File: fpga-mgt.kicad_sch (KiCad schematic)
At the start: 35 parts, among them U34 XCAU25P-2FFVB676I, U39 SI5319C-C-GM-ND, Y4 Resonator_114.285MHZ_ABM8

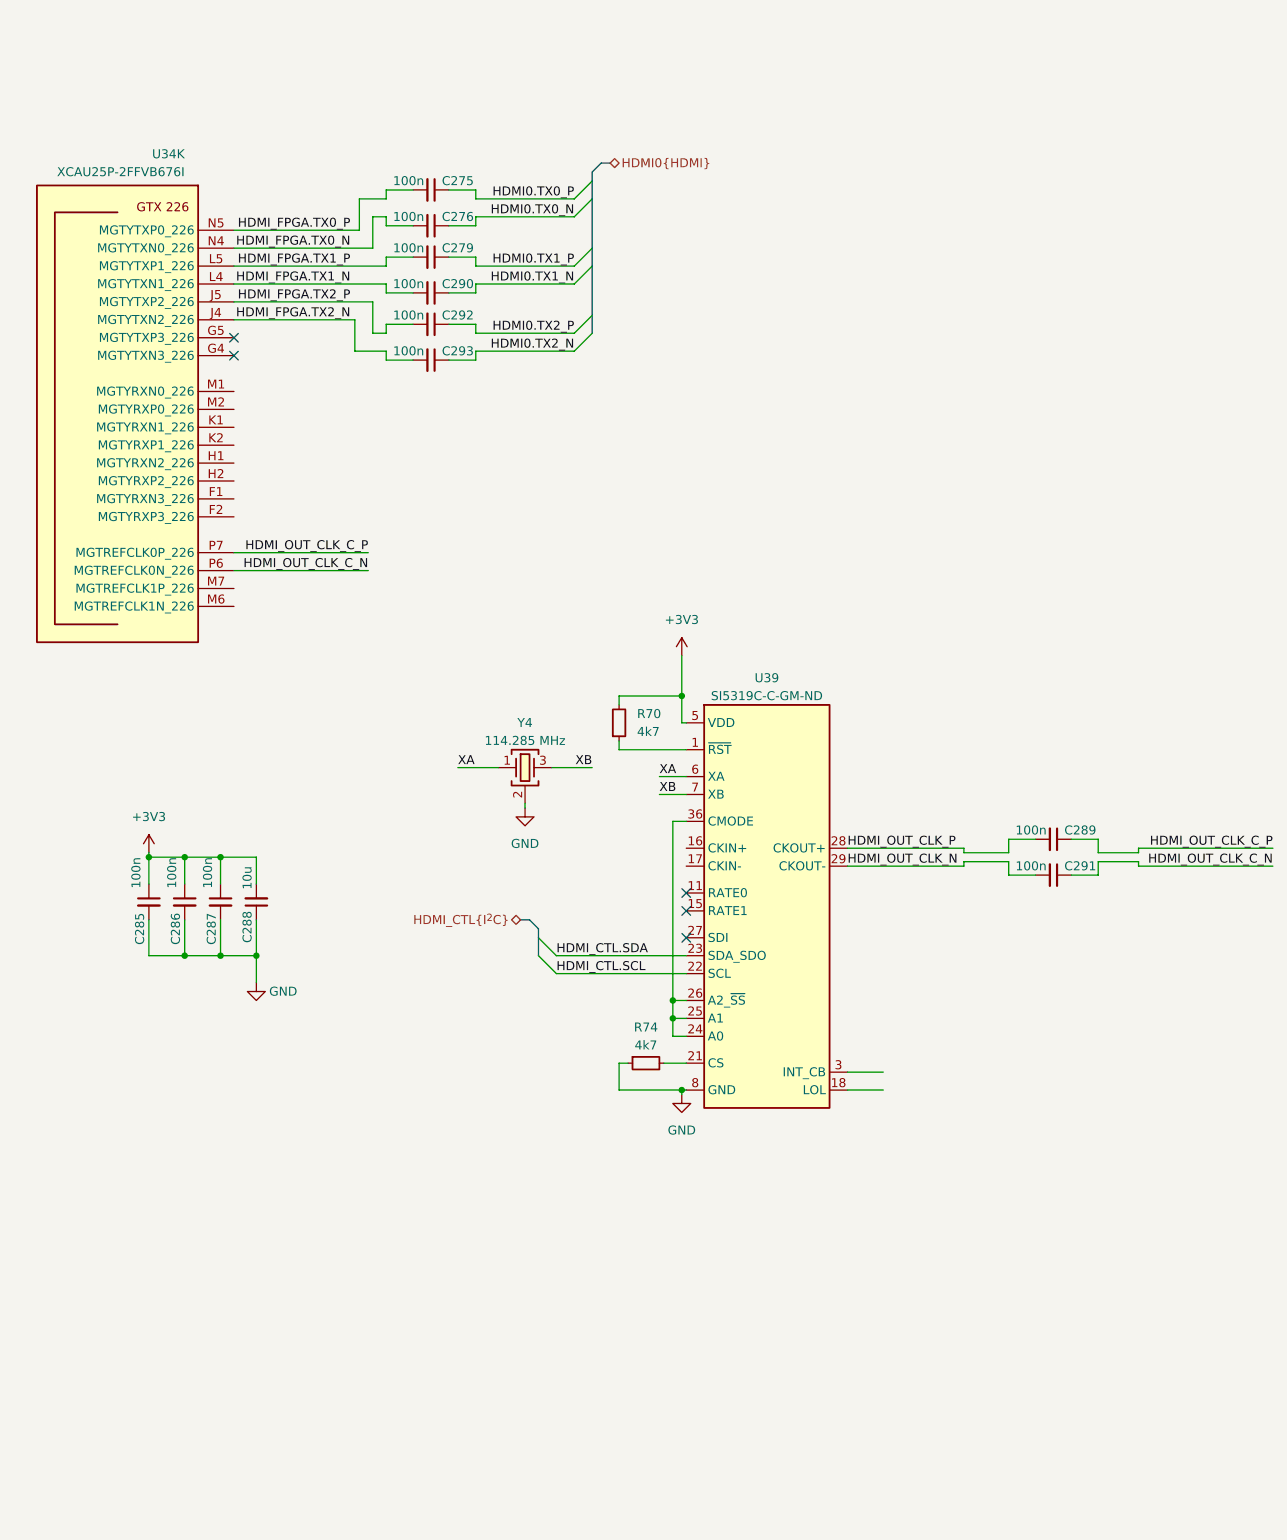
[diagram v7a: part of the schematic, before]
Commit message: [#66311] Start connecting HDMI RX to GTH226 quad
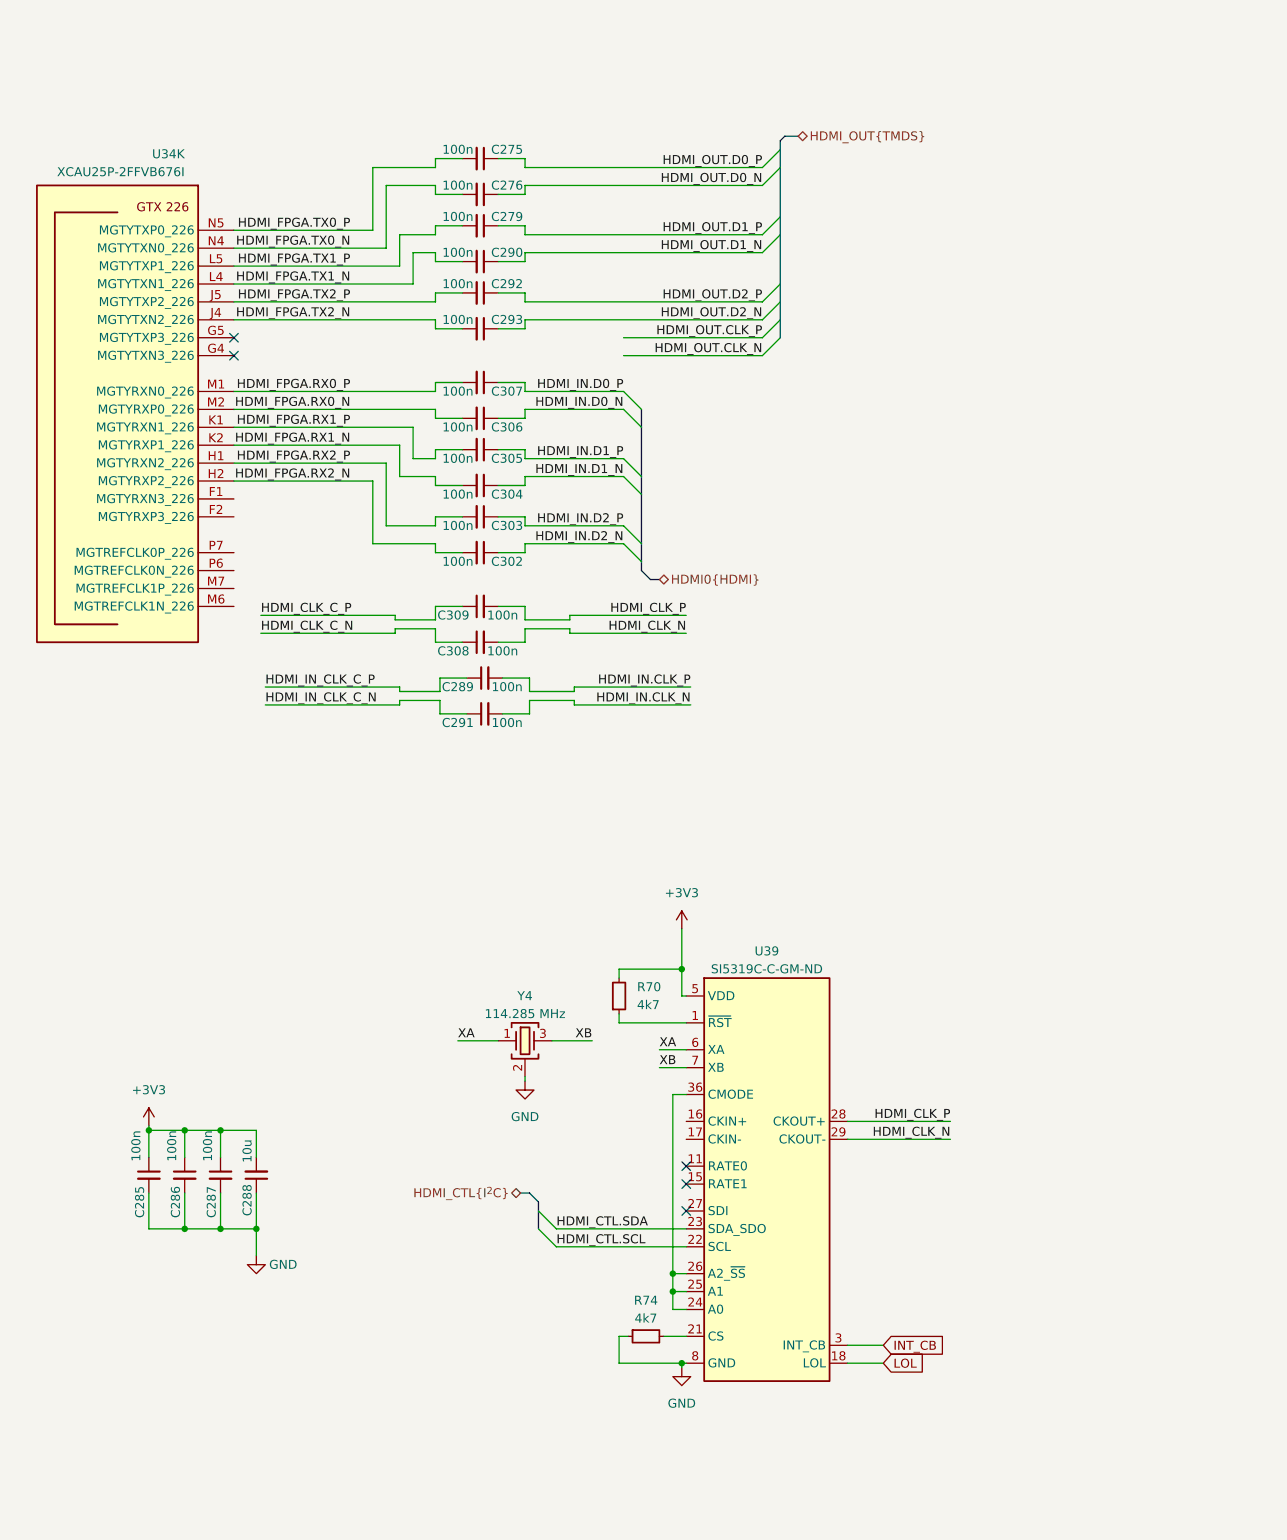
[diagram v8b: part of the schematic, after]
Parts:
- added C302, C303, C304, C305, C306, C307, C308, C309: C_100n_0402, antmicro-footprints:C_0402_1005Metric, symbol antmicroCapacitors0402:C_100n_0402
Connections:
- net HDMI_FPGA.RX2_P: now reaches U34.H1 (MGTYRXN2_226)
- net HDMI_FPGA.RX2_P: now also C303.2
- net HDMI_FPGA.RX2_N: now reaches U34.H2 (MGTYRXP2_226)
- net HDMI_FPGA.RX2_N: now also C302.2
- net HDMI_FPGA.RX1_P: now reaches U34.K1 (MGTYRXN1_226)
- net HDMI_FPGA.RX1_P: now also C305.2
- net HDMI_FPGA.RX1_N: now reaches U34.K2 (MGTYRXP1_226)
- net HDMI_FPGA.RX1_N: now also C304.2
- net HDMI_FPGA.RX0_P: now reaches U34.M1 (MGTYRXN0_226)
- net HDMI_FPGA.RX0_P: now also C307.2
- net HDMI_FPGA.RX0_N: now reaches U34.M2 (MGTYRXP0_226)
- net HDMI_FPGA.RX0_N: now also C306.2
- net LOL: now reaches U39.18 (LOL)
- net INT_CB: now reaches U39.3 (INT_CB)
- net HDMI0.TX0_N renamed HDMI_OUT.D0_N
- net HDMI0.TX0_P renamed HDMI_OUT.D0_P
- net HDMI0.TX1_N renamed HDMI_OUT.D1_N
- net HDMI0.TX1_P renamed HDMI_OUT.D1_P
- net HDMI0.TX2_N renamed HDMI_OUT.D2_N
- net HDMI0.TX2_P renamed HDMI_OUT.D2_P
- net HDMI_OUT_CLK_C_N: no longer names the net of U34.P6 (MGTREFCLK0N_226)
- net HDMI_OUT_CLK_C_N: no longer C291.1
- net HDMI_OUT_CLK_C_P: no longer names the net of U34.P7 (MGTREFCLK0P_226)
- net HDMI_OUT_CLK_C_P: no longer C289.1
- net HDMI_OUT_CLK_N renamed HDMI_CLK_N
- net HDMI_CLK_N: now also C308.2; no longer C291.2
- net HDMI_OUT_CLK_P renamed HDMI_CLK_P
- net HDMI_CLK_P: now also C309.2; no longer C289.2
- new net HDMI_CLK_C_N: C308.1
- new net HDMI_CLK_C_P: C309.1
- new net HDMI_IN.CLK_N: C291.2
- new net HDMI_IN.CLK_P: C289.2
- new net HDMI_IN.D0_N: C306.1
- new net HDMI_IN.D0_P: C307.1
- new net HDMI_IN.D1_N: C304.1
- new net HDMI_IN.D1_P: C305.1
- new net HDMI_IN.D2_N: C302.1
- new net HDMI_IN.D2_P: C303.1
- new net HDMI_IN_CLK_C_N: C291.1
- new net HDMI_IN_CLK_C_P: C289.1
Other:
- moved on the sheet: C275, C276, C279, C285, C286, C287, C288, C290, C292, C293, R70, R74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
